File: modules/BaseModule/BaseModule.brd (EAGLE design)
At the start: 80 x 50 mm, 47 parts, among them IC1 AMS1117-5.0, J1 4P-2.0-90D, J2 4p-2.54

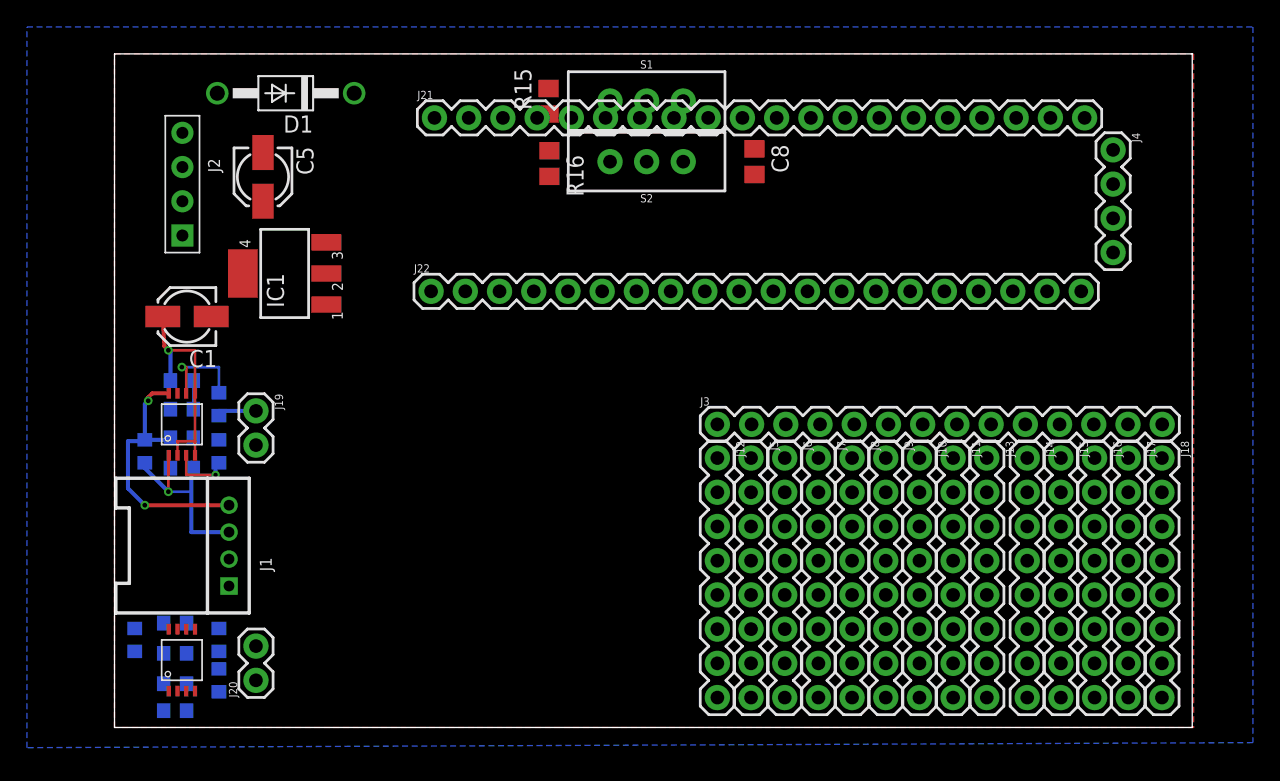
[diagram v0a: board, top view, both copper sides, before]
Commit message: BaseModule pcb updates
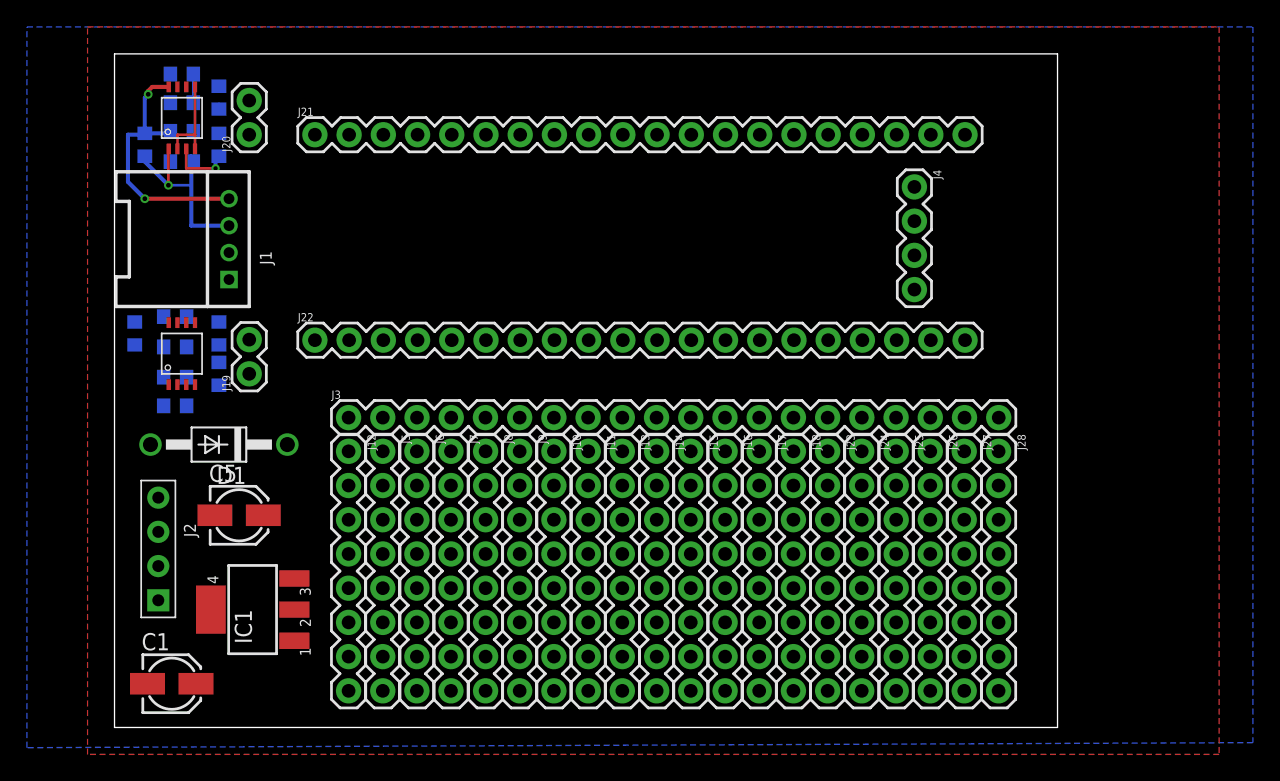
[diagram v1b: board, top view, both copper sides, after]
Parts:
- removed C8: 20pF, rcl:C0805
- removed R15, R16: 100K, rcl:R0805
- removed S1, S2: (no value), SparkFun-Switches:SWITCH_SPDT_PTH_11.6X4.0MM_LOCK
- added J23, J24, J25, J26, J27, J28: (no value), SparkFun-Connectors:1X08
- J3: device SparkFun-Connectors:1X14 -> SparkFun-Connectors:1X20
- moved J20 40.5 mm to (10.0, 44.0)
- moved J14 27.5 mm to (40.2, 20.5)
- moved J15 27.5 mm to (42.8, 20.5)
- moved J16 27.4 mm to (45.3, 20.5)
- moved J17 27.4 mm to (47.9, 20.5)
- moved J12 27.4 mm to (17.4, 20.5)
- moved J3 27.4 mm to (17.4, 23.0)
- moved J18 27.4 mm to (50.4, 20.5)
- moved J5 27.3 mm to (19.9, 20.5)
- moved J6 27.3 mm to (22.4, 20.5)
- moved J7 27.3 mm to (25.0, 20.5)
- moved C1 27.3 mm to (4.25, 3.25), turned to 0 degrees
- moved J8 27.2 mm to (27.5, 20.5)
- moved J9 27.2 mm to (30.1, 20.5)
- moved J10 27.1 mm to (32.6, 20.5)
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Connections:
- removed net BOOT0: R15.1
- removed net BOOT1: R16.2
- removed net N$5: R15.2, S1.2
- removed net N$6: R16.1, S2.2
- new net N$10: J21.9
- new net N$11: J21.10
- new net N$12: J21.11
- new net N$13: J21.12
- new net N$14: J21.13
- new net N$15: J21.14
- new net N$16: J21.15
- new net N$17: J21.16
- new net N$18: J21.17
- new net N$19: J21.18
- new net N$20: J21.19
- new net N$21: J21.20
- new net PB_0: J21.8
- new net PB_1: J21.7
- new net PB_10: J21.6
- new net PB_11: J21.5
- net +3V3: now also J21.3, J22.20; no longer C8.2, S1.1, S2.3
- net +5V: now also J22.18
- net GND: now also J21.1, J21.2, J22.19; no longer C8.1, S1.3, S2.1
- net RX1: no longer R8.2
- net TX2: now also R8.2
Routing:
- net +5V: track 19.2 -> 9.07 mm, vias 1 -> 0
- net N$3: track 6.92 -> 0.00 mm, vias 1 -> 0
- net RX1: track 3.10 -> 0.00 mm
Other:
- board size 80 x 50 mm -> 70 x 50 mm
- board text added: "BaseBoard"
